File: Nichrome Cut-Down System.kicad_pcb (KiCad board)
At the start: 2 copper layers, 48.3 x 47 mm, 18 parts, among them J3 Screw_Terminal_01x03, Q1 Q_PMOS_GDS, Q2 IRLZ44N, SW3 SW_Push_SPDT

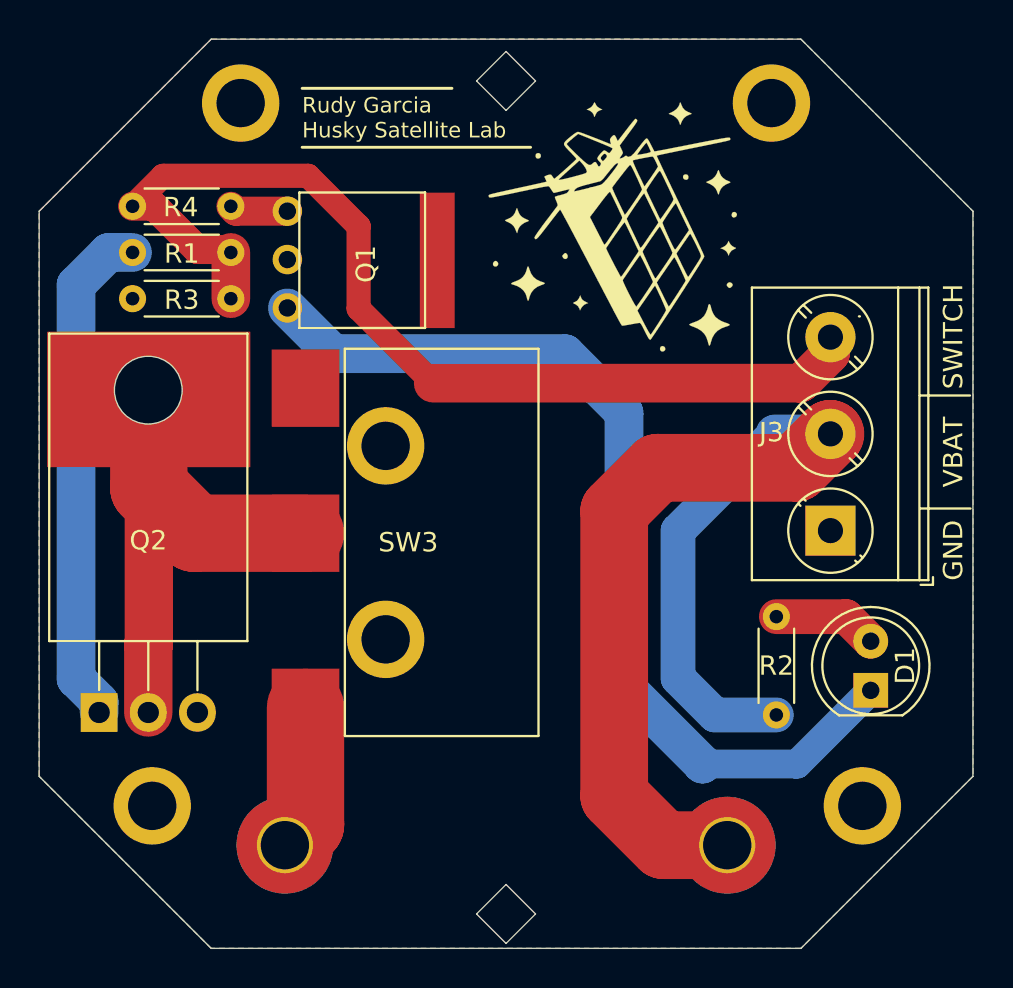
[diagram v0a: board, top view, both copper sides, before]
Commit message: Design Review Changes Implemented
Changed diamond shaped holes to circular shaped holes for fishing line and reducing potential issues with JLCPCB. Also removed MOSFET tab surface mount pad to reduce potential issues with JLCPCB ordering.
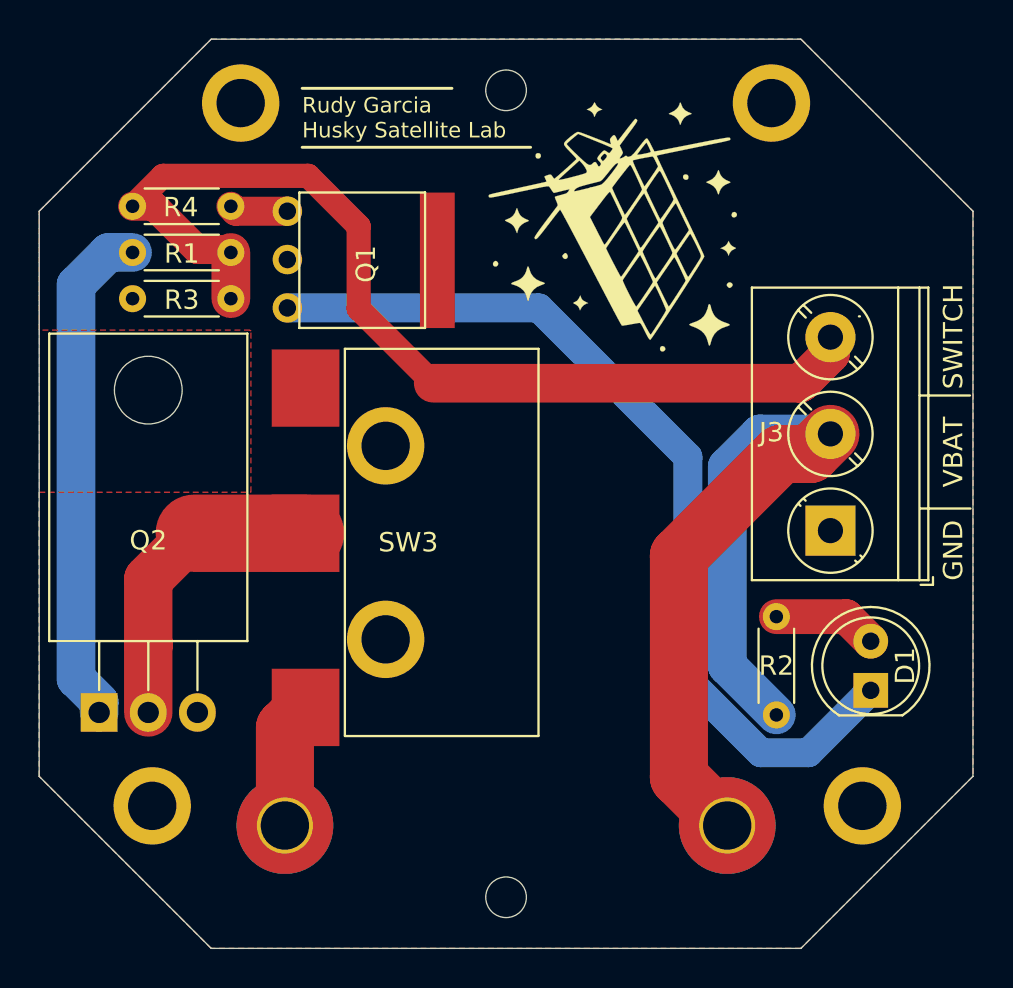
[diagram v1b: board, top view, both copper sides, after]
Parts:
- added REF**: MountingHole_2.1mm, MountingHole:MountingHole_2.1mm, F.Cu at (137.2, 47.1)
- added REF**: MountingHole_2.1mm, MountingHole:MountingHole_2.1mm, F.Cu at (137.2, 88.8)
- moved H1 1.02 mm to (148.6, 85.1)
- moved H2 1.02 mm to (125.7, 85.1)
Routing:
- net VBat: track 57.9 -> 45.3 mm
- net Net-(Q2-Pad2): track 23.7 -> 16.0 mm
- net Net-(D1-Pad1): track 49.8 -> 47.9 mm
- net Net-(H2-Pad1): track 7.56 -> 6.55 mm
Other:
- outline, holes or cut-outs redrawn
